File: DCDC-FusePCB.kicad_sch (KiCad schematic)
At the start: 3 parts, among them J1 Conn_01x02_Socket, J2 Conn_01x02_Socket

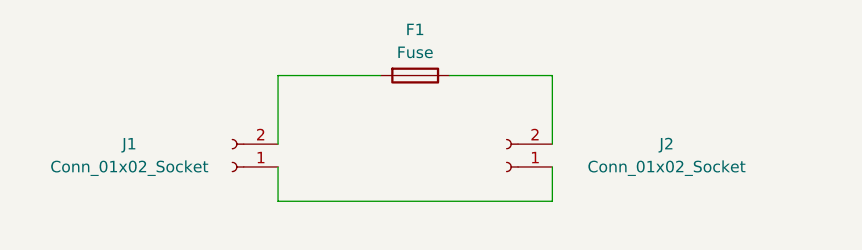
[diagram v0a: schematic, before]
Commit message: replaced conns with screw terminals
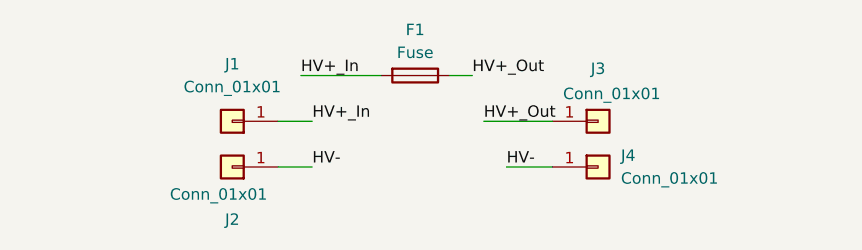
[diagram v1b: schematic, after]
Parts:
- removed J1, J2: Conn_01x02_Socket, Connector_Molex:Molex_Sabre_43160-0102_1x02_P7.49mm_Vertical, symbol Connector:Conn_01x02_Socket
- added J1, J2, J3, J4: Conn_01x01, CustomFootprints:81915, symbol Connector_Generic:Conn_01x01
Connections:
- net HV+_Out: now reaches F1.1
- net HV+_Out: now also J3.1 (Pin_1)
- net HV+_In: now reaches F1.2
- net HV+_In: now also J1.1 (Pin_1)
- new net HV-: J2.1 (Pin_1), J4.1 (Pin_1)

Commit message: mountinghole pads design
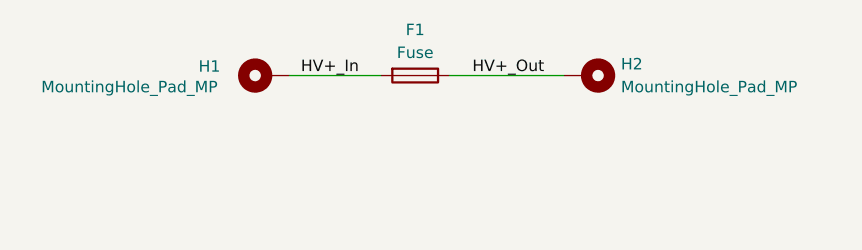
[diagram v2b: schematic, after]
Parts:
- removed J1, J2, J3, J4: Conn_01x01, CustomFootprints:81915, symbol Connector_Generic:Conn_01x01
- added H1, H2: MountingHole_Pad_MP, MountingHole:MountingHole_8.4mm_M8_Pad_TopBottom, symbol Mechanical:MountingHole_Pad_MP
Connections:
- net HV+_In: now also H1.MP
- net HV+_Out: now also H2.MP
